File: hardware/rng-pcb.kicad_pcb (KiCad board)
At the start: 2 copper layers, 54.6 x 72 mm, 46 parts, among them J1 USB_B_Micro, J2 OLED, J3 Conn_01x01_Male, J4 Conn_01x01_Male, J5 Conn_01x01_Male, J6 Conn_01x01_Male, Q1 MMBT3904, Q2 MMBT3904, Q3 MMBT3904, SW1 SW_Push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

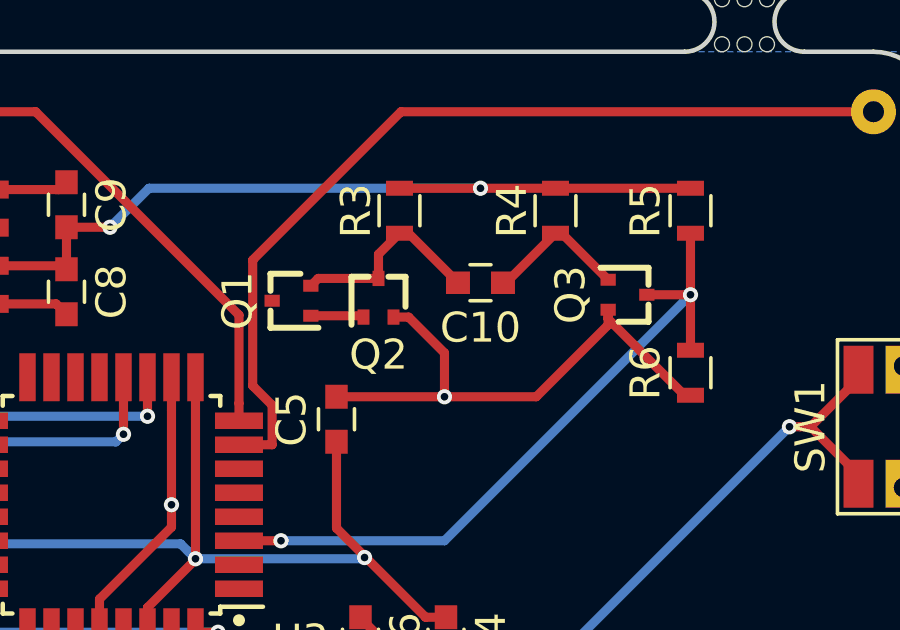
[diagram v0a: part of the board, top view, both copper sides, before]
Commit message: BOM updates, footprints changed
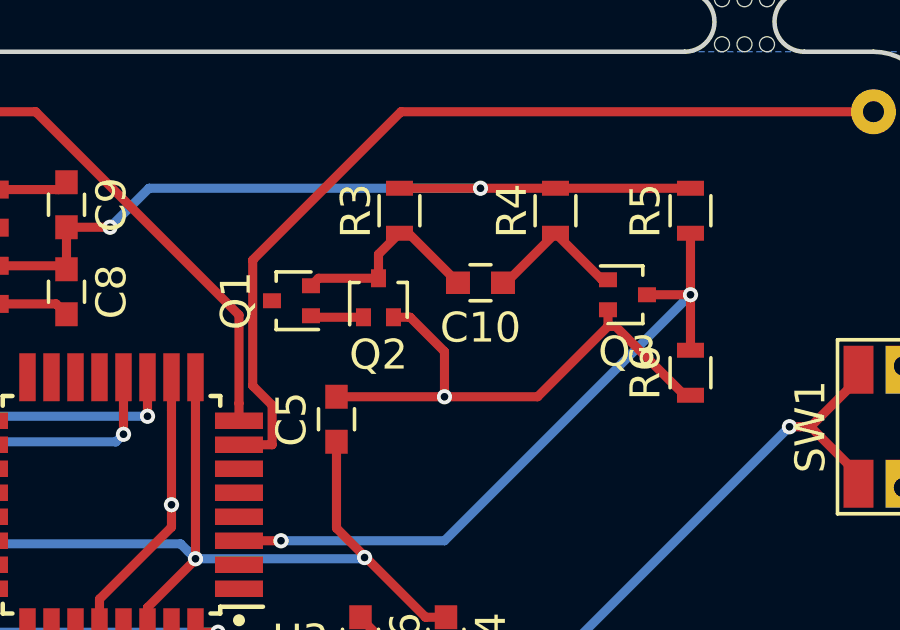
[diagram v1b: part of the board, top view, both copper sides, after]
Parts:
- Q1, Q2, Q3: footprint rng-pcb:SOT523 -> Package_TO_SOT_SMD:SOT-416
- turned Q1 to 180 degrees
- turned Q2 to 90 degrees
- turned Q3 to 0 degrees
